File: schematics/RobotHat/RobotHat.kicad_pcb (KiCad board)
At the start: 2 copper layers, 37 parts, among them J1 9Vin, J10 MotorB, J2 ATMega_ICSP, J3 ATMega_FTDI, J4 I2C, J5 Raspberry_Pi_2_3, J6 ATMega AnalogPins, J7 WheelEncA, J8 WheelEncB, J9 MotorA, SW1 Reset, U1 ATmega328P-MU, U2 MIC5205-5.0YM5, U3 TB6612FNG, Y1 16MHz

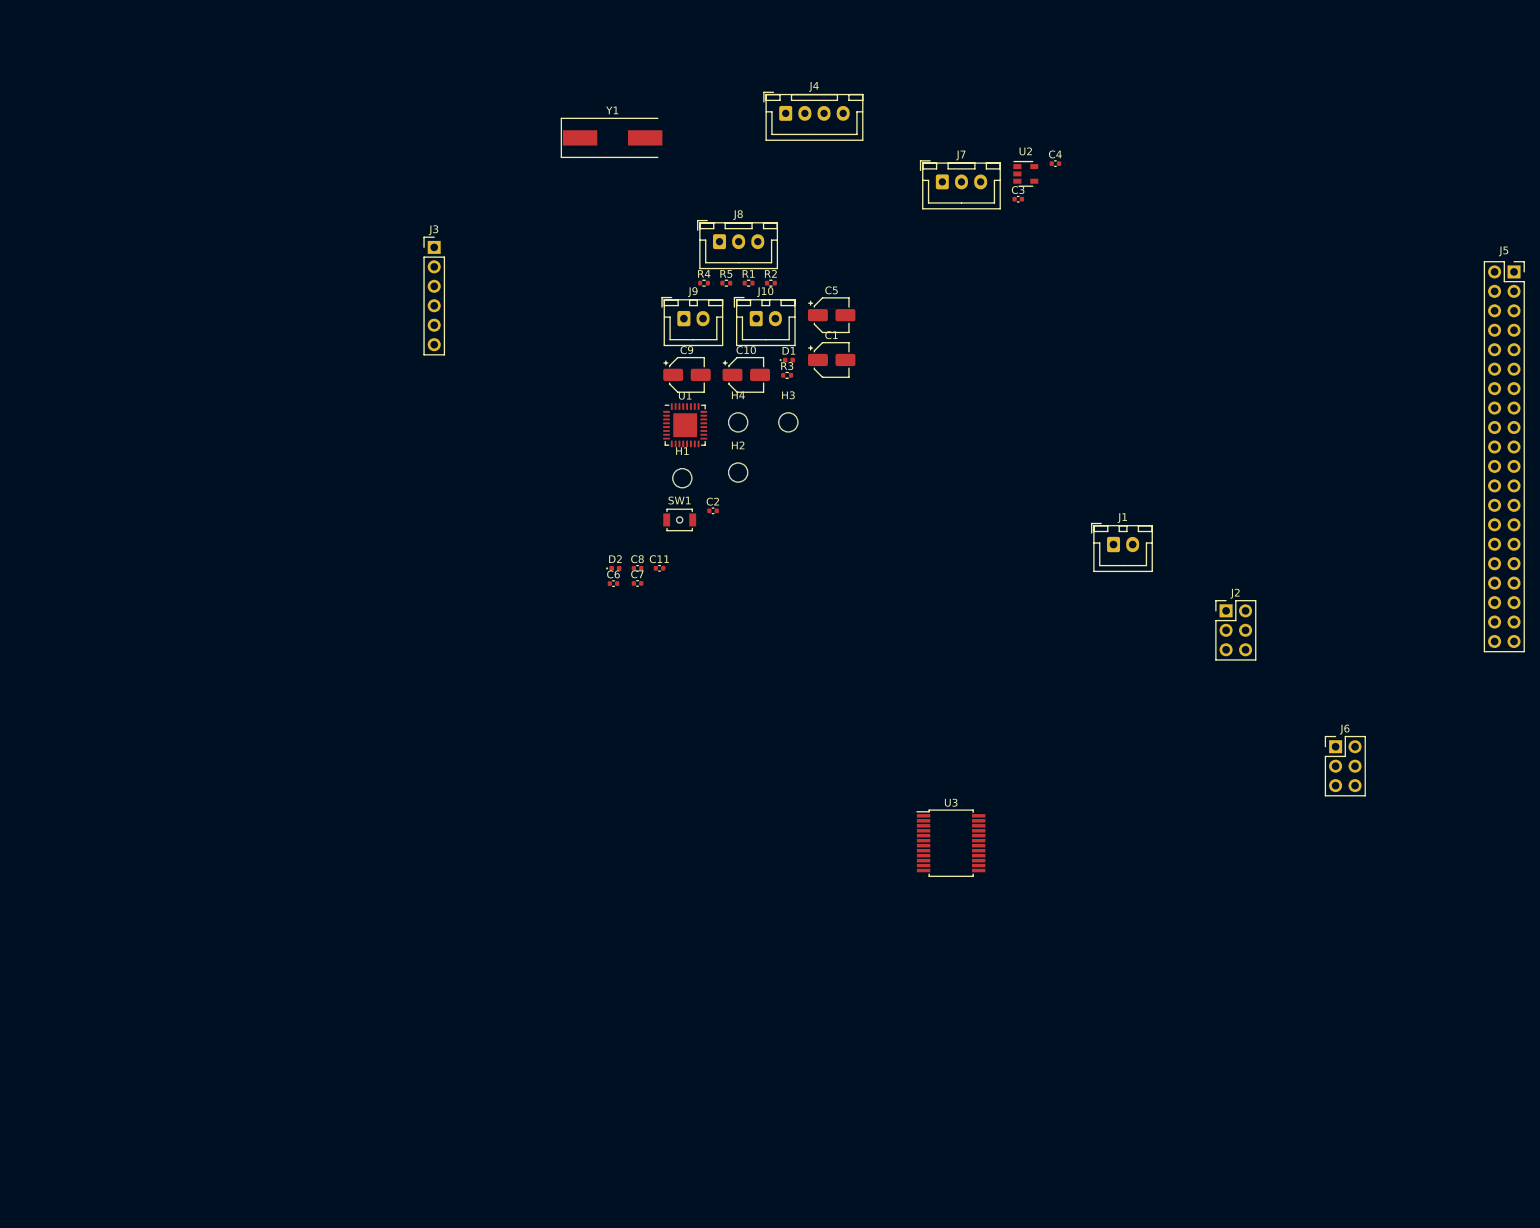
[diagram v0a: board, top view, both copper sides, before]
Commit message: Added robot hat
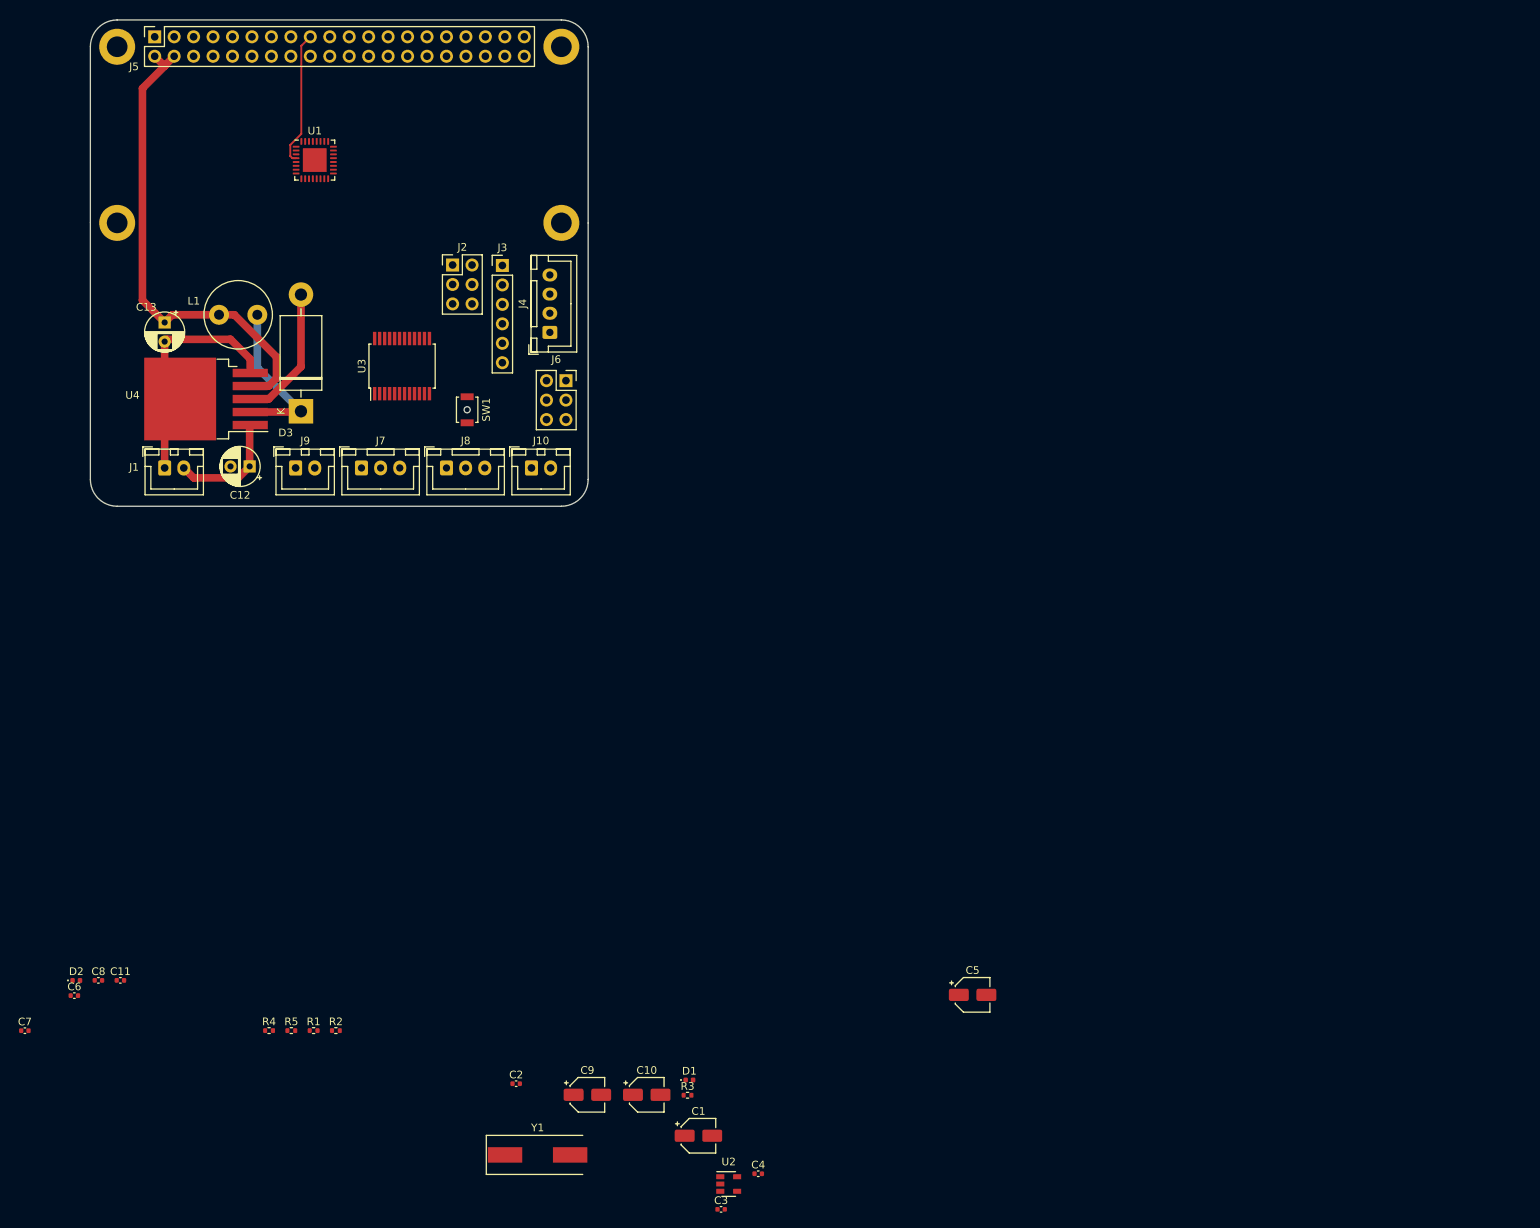
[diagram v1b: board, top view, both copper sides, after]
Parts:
- added C12: 100uF, Capacitor_THT:CP_Radial_D5.0mm_P2.50mm, F.Cu at (71.1, 100.3)
- added C13: 220uf, Capacitor_THT:CP_Radial_D5.0mm_P2.50mm, F.Cu at (60.0, 81.5)
- added D3: 1N5822, Diode_THT:D_DO-201AD_P15.24mm_Horizontal, F.Cu at (77.8, 93.1)
- added L1: 33uH, Inductor_THT:L_Radial_D8.7mm_P5.00mm_Fastron_07HCP, F.Cu at (67.1, 80.5)
- added U4: LM2596S-5, Package_TO_SOT_SMD:TO-263-5_TabPin3, F.Cu at (65.4, 91.5)
- H1, H2, H3, H4: footprint MountingHole:MountingHole_2.5mm -> MountingHole:MountingHole_2.7mm_M2.5_DIN965_Pad
- J6: footprint Connector_PinHeader_2.54mm:PinHeader_2x03_P2.54mm_Vertical -> Connector_PinSocket_2.54mm:PinSocket_2x03_P2.54mm_Vertical
- moved J5 180.1 mm to (58.7, 44.2), turned to 90 degrees
- moved C3 137.5 mm to (132.7, 197.3)
- moved C4 137.5 mm to (137.5, 192.7)
- moved U2 137.5 mm to (133.7, 194.0)
- moved Y1 133.2 mm to (108.7, 190.2)
- moved J1 124.3 mm to (60.0, 100.5)
- moved R4 112.9 mm to (73.6, 174.0)
- moved R1 112.9 mm to (79.5, 174.0)
- moved R2 112.9 mm to (82.4, 174.0)
- moved R5 112.9 mm to (76.5, 174.0)
- moved J6 111.3 mm to (112.4, 89.1)
- moved J2 110.6 mm to (97.6, 74.0)
- moved C1 102.8 mm to (129.7, 187.7)
- moved C7 99.0 mm to (41.8, 174.0)
- moved U3 95.0 mm to (91.0, 87.2), turned to 90 degrees
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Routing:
- net +5V: track 0.00 -> 63.4 mm
- net GND: track 0.00 -> 50.2 mm
- net Net-(D3-Pad1): track 0.00 -> 21.6 mm
- net +3V3: track 0.00 -> 17.5 mm
- net +9V: track 0.00 -> 15.2 mm
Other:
- board outline added: 65 x 63.5 mm

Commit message: Completed Robot Had for RaspberryPi
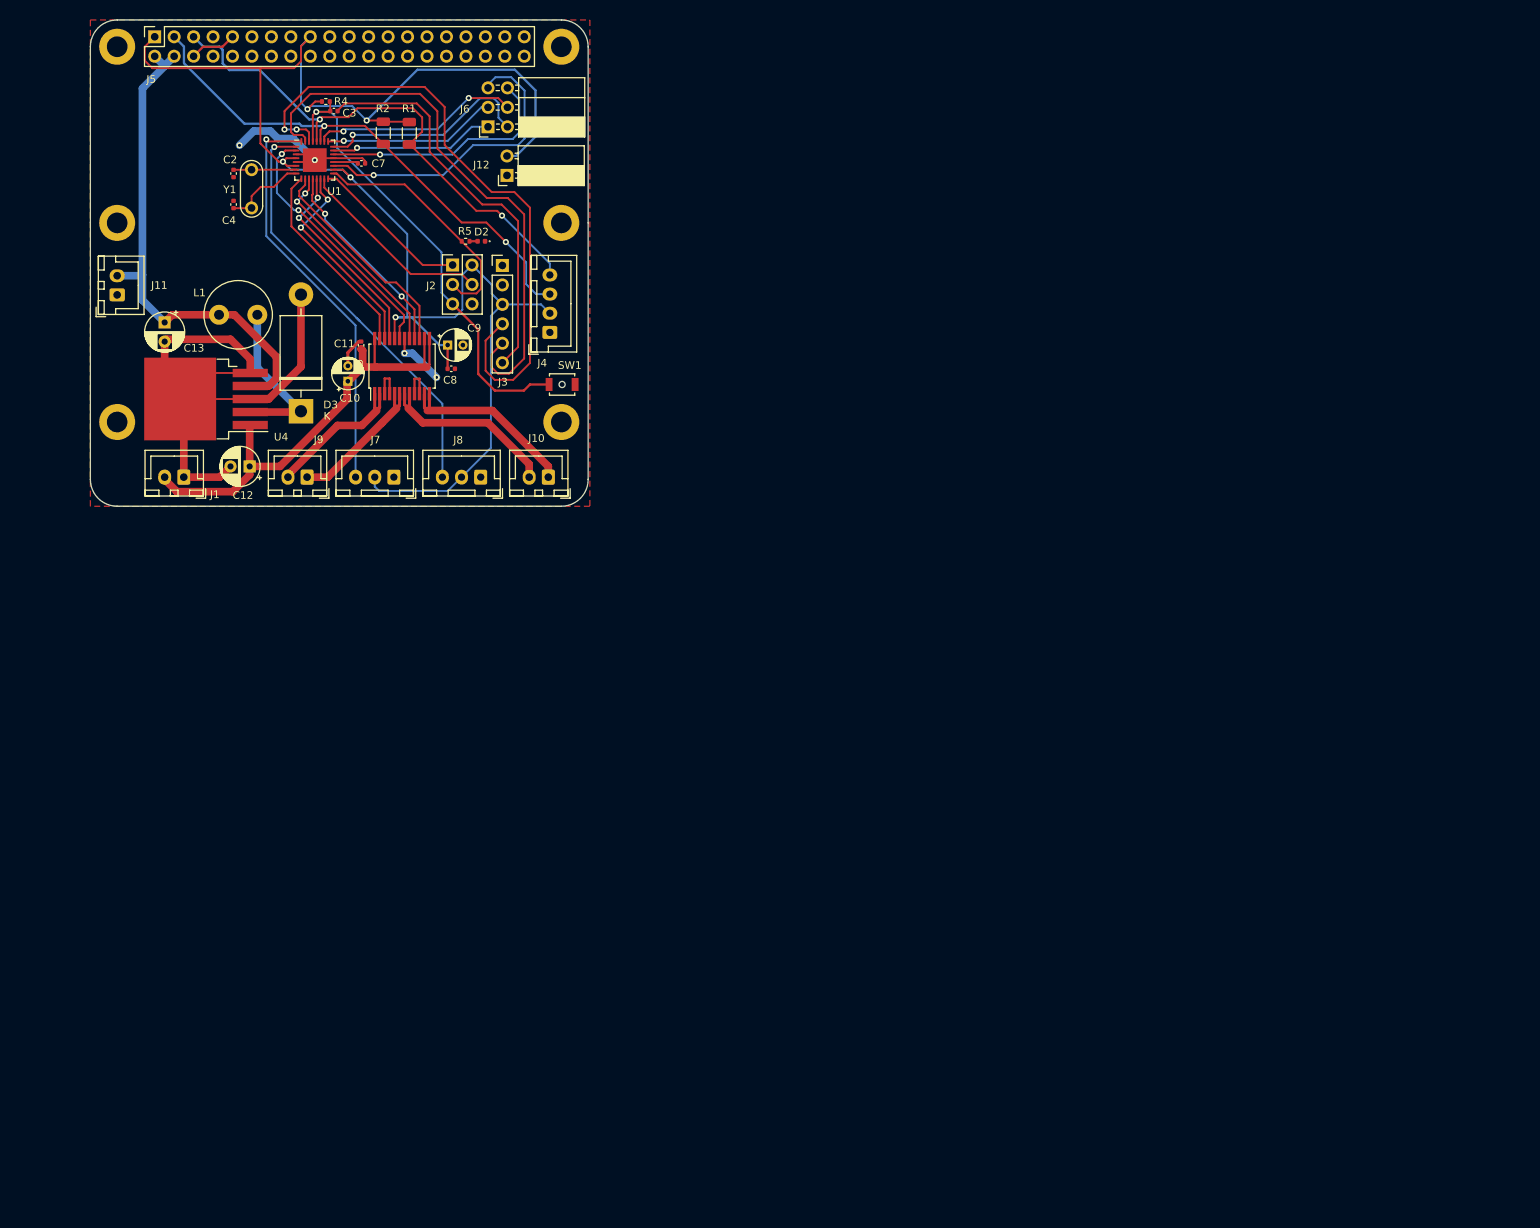
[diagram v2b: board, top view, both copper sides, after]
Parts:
- removed C1, C5: 10uF, Capacitor_SMD:CP_Elec_4x5.4
- removed C6: 0.1uF, Capacitor_SMD:C_0402_1005Metric
- removed D1: RED, Diode_SMD:D_0402_1005Metric
- removed R3: 10k, Resistor_SMD:R_0402_1005Metric
- removed U2: MIC5205-5.0YM5, Package_TO_SOT_SMD:SOT-23-5
- added H5: MountingHole, MountingHole:MountingHole_2.7mm_M2.5_DIN965_Pad, F.Cu at (53.8, 94.5)
- added H6: MountingHole, MountingHole:MountingHole_2.7mm_M2.5_DIN965_Pad, F.Cu at (111.8, 94.5)
- added J11: 5Vout, Connector_JST:JST_XH_B2B-XH-A_1x02_P2.50mm_Vertical, F.Cu at (53.8, 77.9)
- added J12: 3V3out, Connector_PinSocket_2.54mm:PinSocket_1x02_P2.54mm_Horizontal, F.Cu at (104.7, 62.3)
- C10, C9: footprint Capacitor_SMD:CP_Elec_4x5.4 -> Capacitor_THT:CP_Radial_D4.0mm_P2.00mm
- J6: footprint Connector_PinSocket_2.54mm:PinSocket_2x03_P2.54mm_Vertical -> Connector_PinSocket_2.54mm:PinSocket_2x03_P2.54mm_Horizontal
- R1, R2: footprint Resistor_SMD:R_0402_1005Metric -> Resistor_SMD:R_1206_3216Metric
- Y1: footprint Crystal:Crystal_SMD_HC49-SD -> Crystal:Resonator-2Pin_W7.0mm_H2.5mm
- moved C3 152.1 mm to (82.1, 53.9), turned to 180 degrees
- moved C4 143.9 mm to (69.0, 66.1), turned to 270 degrees
- moved Y1 129.2 mm to (71.3, 66.5), turned to 90 degrees
- moved C2 124.4 mm to (69.0, 62.0), turned to 90 degrees
- moved R4 121.5 mm to (81.0, 52.6)
- moved C7 121.5 mm to (85.7, 60.7), turned to 180 degrees
- moved R1 117.8 mm to (92.0, 56.8), turned to 270 degrees
- moved R2 117.4 mm to (88.5, 56.8), turned to 270 degrees
- moved D2 110.1 mm to (101.3, 70.9), turned to 180 degrees
- moved R5 105.6 mm to (99.3, 70.9)
- moved C10 101.0 mm to (83.9, 89.2), turned to 90 degrees
- moved C9 99.6 mm to (97.0, 84.5)
- moved C8 92.2 mm to (97.4, 87.5)
- moved C11 88.7 mm to (85.7, 84.5), turned to 90 degrees
- moved J6 34.7 mm to (102.2, 56.0), turned to 180 degrees
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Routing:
- net +3V3: track 17.5 -> 226.9 mm, vias 0 -> 5
- net RXI: track 0.00 -> 84.3 mm, vias 0 -> 2
- net GND: track 50.2 -> 131.3 mm, vias 0 -> 4
- net TXO: track 0.00 -> 73.9 mm
- net SCL: track 0.00 -> 70.0 mm, vias 0 -> 2
- net SDA: track 0.00 -> 68.2 mm, vias 0 -> 2
- net RESET: track 0.00 -> 61.8 mm, vias 0 -> 1
- net D3: track 0.00 -> 56.0 mm, vias 0 -> 1
- net D2: track 0.00 -> 53.6 mm, vias 0 -> 1
- net DTR: track 0.00 -> 52.5 mm
- net +9V: track 15.2 -> 63.3 mm
- net A6: track 0.00 -> 40.3 mm, vias 0 -> 1
- net D4: track 0.00 -> 33.9 mm, vias 0 -> 2
- net SCK: track 0.00 -> 32.1 mm
- net A7: track 0.00 -> 31.9 mm, vias 0 -> 1
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- added copper zone on F.Cu, net GND

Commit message: Re organizing
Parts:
- added C10: 0.1uf, Capacitor_SMD:C_1206_3216Metric, F.Cu at (96.3, 94.5)
- added D1: SS34, RobotHat:SS34, F.Cu at (77.2, 91.3)
- added R5: 330, Resistor_SMD:R_0402_1005Metric, F.Cu at (55.8, 82.2)
- C11: footprint Capacitor_SMD:C_0402_1005Metric -> Capacitor_SMD:C_1206_3216Metric
- C7: renamed from C8; footprint Capacitor_SMD:C_0402_1005Metric -> Capacitor_SMD:C_1206_3216Metric
- C9: value 10uf -> 0.1uf; footprint Capacitor_THT:CP_Radial_D4.0mm_P2.00mm -> Capacitor_SMD:C_1206_3216Metric
- D3: value 1N5822 -> RED; footprint Diode_THT:D_DO-201AD_P15.24mm_Horizontal -> Diode_SMD:D_0402_1005Metric
- Y1: footprint Crystal:Resonator-2Pin_W7.0mm_H2.5mm -> Crystal:Crystal_HC49-4H_Vertical
- moved D3 27.0 mm to (53.1, 82.2), turned to 0 degrees
- moved C9 14.0 mm to (87.7, 95.0)
- moved J6 7.15 mm to (111.5, 75.8), turned to 270 degrees
- moved C7 2.90 mm to (96.9, 84.7), turned to 270 degrees
- moved C11 1.39 mm to (85.1, 83.2)
- moved C4 1.30 mm to (67.7, 66.1)
- moved C2 1.20 mm to (67.8, 62.0)
- renumbered C12 to C1, C13 to C5, C7 to C6, C10 to C8, J9 to J10, J10 to J11, J5 to J12, J11 to J2, J12 to J3, J2 to J4, J3 to J5, J4 to J6, J6 to J7, J7 to J8, J8 to J9, R4 to R3, R5 to R4, U4 to U2
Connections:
- C9 pad 1: +3V3 -> MOTORA1
- C9 pad 2: GND -> MOTORA2
- D3 pad 1: Net-(D3-Pad1) -> GND
- D3 pad 2: GND -> Net-(D3-Pad2)
- L1 pad 2: Net-(D3-Pad1) -> Net-(D1-Pad1)
- U2 pad 2: Net-(D3-Pad1) -> Net-(D1-Pad1)
- U3 pad 15: D6 -> D10
- U3 pad 16: D8 -> D9
- U3 pad 17: D7 -> D8
- U3 pad 21: D9 -> D7
- U3 pad 22: D10 -> D6
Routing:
- net +3V3: track 226.9 -> 264.6 mm, vias 5 -> 6
- net GND: track 131.3 -> 162.4 mm, vias 4 -> 10
- net Net-(D1-Pad1): track 0.00 -> 22.5 mm
- net Net-(D3-Pad1): track 21.6 -> 0.00 mm
- net SCL: track 70.0 -> 81.4 mm
- net SDA: track 68.2 -> 74.7 mm
- net +5V: track 66.7 -> 70.7 mm
- net D3: track 56.0 -> 59.1 mm
- net D2: track 53.6 -> 56.4 mm
- net D8: track 26.5 -> 29.2 mm, vias 2 -> 0
- net XTAL1: track 8.17 -> 10.7 mm
- net D6: track 28.5 -> 26.0 mm
- net D4: track 33.9 -> 36.4 mm
- net Net-(D3-Pad2): track 0.00 -> 1.74 mm
- net D7: track 27.7 -> 26.0 mm, vias 2 -> 0
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- added copper zone on B.Cu, net GND
